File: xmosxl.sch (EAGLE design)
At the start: 1 part

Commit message: Add the block diagram
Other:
- note added: "!MPD!, !EXTSEL!"
- note added: "0.035mm"
- note added: "0.11mm pre-preg"
- note added: "0.12mm pre-preg"
- note added: "0.53mm pre-preg"
- note added: "177ns"
- note added: "225ns"
- note added: "3.96"
- note added: "4.29"
- note added: "422ns"
- note added: "486ns"
- note added: "Address,Data, Control from Mini-SAS"
- note added: "Atari Bus Mini-SAS (5v)"
- note added: "CLK"
- note added: "Cycle time = 558ns"
- note added: "Debug / XTAG / Link / UART"
- note added: "Dielectric constant"
- note added: "Expansion: bus + link (5w)"
- note added: "GND"
- note added: "I2C"
- note added: "Layer stack-up"
- note added: "Level Convert 5v <--> 3.3v"
- note added: "Per slot !IRQ!"
- note added: "Read"
- note added: "Shared A/D/State bus"
- note added: "Shared SPI / SS per slot"
- note added: "Signal"
- note added: "Slots"
- note added: "UART"
- note added: "VDD"
- note added: "Valid address"
- note added: "Write"
- note added: "XMOS 4-tile CPU - 2-way link to debugger - 5-way link to expansion - I2C / Uart offered - A/D/Flags bus decodes A8 bus - Expansion connector - SPI interface to slots"
- note added: "miniPBI+ (5v)"

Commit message: Start to lay out the design. Add slots and holes to take up space, and start to populate the level converters / vregs
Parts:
- added A8_CONN: MINI-SAS, sjg-con:MINI-SAS
- added AUDIO: AUDIO, pinhead:PINHD-1X3
- added C1, C10, C11, C12, C13, C14, C15, C16, C17, C18, C19, C2, C20, C3, C4, C5, C51, C52, C6, C7, C8, C9: 0.1uF, rcl:C-EUC0201
- added C21, C22, C23, C24, C25, C26, C27, C28, C29, C30, C31, C32, C33, C34, C35, C36, C37, C38, C39, C40, C43: 0.1uF, rcl:C-EUC0402K
- added C41, C42, C44, C45, C47: 10uF, rcl:C-EUC0402K
- added C46, C48: 1uF, rcl:C-EUC0402K
- added C49: 0.1uF, rcl:C-EUC0402
- added C50: 120pF, rcl:C-EUC0402
- added H1, H2, H3, H4: MOUNT-HOLE3.2, holes:MOUNT-HOLE3.2
- added IC1, IC2, IC3, IC4, IC5, IC8, IC9: 74LVC1T45W6-7, samacsys:74LVC1T45W6-7
- added IC6, IC7: 74ALVC164245DGG_11, samacsys:74ALVC164245DGG_11
- added PJ-102AH: PJ-102AH, adafruit:2.1MMJACKTHM
- added R1, R11, R2, R3, R4, R5, R6, R7, R8, R9: 10K, rcl:R-EU_R0201
- added R10: 47K, rcl:R-EU_R0402
- added SLOT1, SLOT2, SLOT3, SLOT4, SLOT5, SLOT6: PCIE_64, pcie:PCIE_64
- added U$2: AP7363-330-13, sjg-power:AP7363
- added U$3: LD49300, sjg-power:LD49150
- added U$4: TPS3808G33DBVR, sjg-power:TPS3808DBVR
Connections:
- new net !EXTSEL!: IC9.B
- new net !EXTSEL!_DIR: IC9.DIR, R11.2
- new net !HALT!: IC4.B
- new net !HALT!_DIR: IC4.DIR, R7.1
- new net !HI_EXTSEL!: A8_CONN.B13, IC9.A
- new net !HI_HALT!: A8_CONN.A14, IC4.A
- new net !HI_IRQ!: A8_CONN.B14, IC3.A
- new net !HI_MPD!: A8_CONN.A15, IC5.A
- new net !HI_REF!: A8_CONN.B16, IC8.A
- new net !HI_RST!: A8_CONN.A17, IC2.A
- new net !IRQ!: IC3.B
- new net !IRQ!_DIR: IC3.DIR, R6.1
- new net !MPD!: IC5.B
- new net !MPD!_DIR: IC5.DIR, R8.1
- new net !REF!: IC8.B
- new net !REF!_DIR: IC8.DIR, R9.1
- new net !RST!: IC2.B
- new net !RST!_DIR: IC2.DIR, R5.1
- new net +3V3: C10.1, C14.1, C15.1, C16.1, C19.1, C20.1, C21.1, C22.1, C23.1, C24.1, C25.1, C26.1, C27.1, C28.1, C41.1, C43.1, C45.1, C49.1, C52.1, C6.1, C7.1, C8.1, C9.1, IC1.VCC(B), IC2.VCC(B), IC3.VCC(B), IC4.VCC(B), IC5.VCC(B), IC6.VCC(A)@31, IC6.VCC(A)@42, IC7.VCC(A)@31, IC7.VCC(A)@42, IC8.VCC(B), IC9.VCC(B), R1.2, R10.2, R11.1, R5.2, R6.2, R7.2, R8.2, R9.2, U$1-POWER.VDDIO@A11, U$1-POWER.VDDIO@A2, U$1-POWER.VDDIO@A20, U$1-POWER.VDDIO@AA11, U$1-POWER.VDDIO@AA2, U$1-POWER.VDDIO@AA20, U$1-POWER.VDDIO@D7, U$1-POWER.VDDIO@E15, U$1-POWER.VDDIO@E7, U$1-POWER.VDDIO@F2, U$1-POWER.VDDIO@F20, U$1-POWER.VDDIO@L1, U$1-POWER.VDDIO@L21, U$1-POWER.VDDIO@T2, U$1-POWER.VDDIO@T20, U$1-POWER.VDDIO@U11, U$1-POWER.VDDIO@U15, U$1-POWER.VDDIO@U7, U$1-POWER.VDDIOT@A16, U$1-POWER.VDDIOT@A6, U$2.OUT@3, U$4.SENSE@5, U$4.VDD@6
- new net +5V: C1.1, C11.1, C12.1, C13.1, C17.1, C18.1, C2.1, C3.1, C4.1, C44.1, C46.1, C48.1, C5.1, C51.1, IC1.VCC(A), IC2.VCC(A), IC3.VCC(A), IC4.VCC(A), IC5.VCC(A), IC6.VCC(B)@18, IC6.VCC(B)@7, IC7.VCC(B)@18, IC7.VCC(B)@7, IC8.VCC(A), IC9.VCC(A), PJ-102AH.TIP, U$2.IN@1, U$3.VBIAS, U$3.VIN
- new net A0: IC7.1A0
- new net A1: IC7.1A1
- new net A10: IC7.2A2
- new net A11: IC7.2A3
- new net A12: IC7.2A4
- new net A13: IC7.2A5
- new net A14: IC7.2A6
- new net A15: IC7.2A7
- new net A2: IC7.1A2
- new net A3: IC7.1A3
- new net A4: IC7.1A4
- new net A5: IC7.1A5
- new net A6: IC7.1A6
- new net A7: IC7.1A7
- new net A8: IC7.2A0
- new net A9: IC7.2A1
- new net AUDIO_L: A8_CONN.B18, AUDIO.3
- new net AUDIO_R: A8_CONN.A18, AUDIO.1
- new net A_DIR: IC7.1DIR, IC7.2DIR, R2.1
- new net CLK: IC6.2A2
- new net CTRL_DIR: IC6.2DIR, R4.1
- new net D0: IC6.1A0
- new net D1: IC6.1A1
- new net D2: IC6.1A2
- new net D3: IC6.1A3
- new net D4: IC6.1A4
- new net D5: IC6.1A5
- new net D6: IC6.1A6
- new net D7: IC6.1A7
- new net D_DIR: IC6.1DIR, R3.1
- new net EN_1V0: R10.1, U$3.EN, U$4.!RESET!@1
- new net GND: A8_CONN.SHIELD, AUDIO.2, C1.2, C10.2, C11.2, C12.2, C13.2, C14.2, C15.2, C16.2, C17.2, C18.2, C19.2, C2.2, C20.2, C21.2, C22.2, C23.2, C24.2, C25.2, C26.2, C27.2, C28.2, C29.2, C3.2, C30.2, C31.2, C32.2, C33.2, C34.2, C35.2, C36.2, C37.2, C38.2, C39.2, C4.2, C40.2, C41.2, C42.2, C43.2, C44.2, C45.2, C46.2, C47.2, C48.2, C49.2, C5.2, C50.2, C51.2, C52.2, C6.2, C7.2, C8.2, C9.2, IC1.GND, IC2.GND, IC3.GND, IC4.GND, IC5.GND, IC6.!1OE, IC6.!2OE, IC6.2A3, IC6.2A4, IC6.2A5, IC6.2A6, IC6.2A7, IC6.2B3, IC6.2B4, IC6.2B5, IC6.2B6, IC6.2B7, IC6.GND@10, IC6.GND@15, IC6.GND@21, IC6.GND@28, IC6.GND@34, IC6.GND@39, IC6.GND@4, IC6.GND@45, IC7.!1OE, IC7.!2OE, IC7.GND@10, IC7.GND@15, IC7.GND@21, IC7.GND@28, IC7.GND@34, IC7.GND@39, IC7.GND@4, IC7.GND@45, IC8.GND, IC9.GND, PJ-102AH.RING, R2.2, R3.2, R4.2, U$1-POWER.GND@A1, U$1-POWER.GND@A21, U$1-POWER.GND@AA1, U$1-POWER.GND@AA21, U$1-POWER.GND@B11, U$1-POWER.GND@C15, U$1-POWER.GND@C7, U$1-POWER.GND@D6, U$1-POWER.GND@E16, U$1-POWER.GND@E6, U$1-POWER.GND@F19, U$1-POWER.GND@F3, U$1-POWER.GND@J13, U$1-POWER.GND@J14, U$1-POWER.GND@J15, U$1-POWER.GND@J16, U$1-POWER.GND@J17, U$1-POWER.GND@J5, U$1-POWER.GND@J6, U$1-POWER.GND@J7, U$1-POWER.GND@J8, U$1-POWER.GND@J9, U$1-POWER.GND@K13, U$1-POWER.GND@K14, U$1-POWER.GND@K15, U$1-POWER.GND@K16, U$1-POWER.GND@K17, U$1-POWER.GND@K5, U$1-POWER.GND@K6, U$1-POWER.GND@K7, U$1-POWER.GND@K8, U$1-POWER.GND@K9, U$1-POWER.GND@L13, U$1-POWER.GND@L14, U$1-POWER.GND@L15, U$1-POWER.GND@L16, U$1-POWER.GND@L17, U$1-POWER.GND@L2, U$1-POWER.GND@L20, U$1-POWER.GND@L5, U$1-POWER.GND@L6, U$1-POWER.GND@L7, U$1-POWER.GND@L8, U$1-POWER.GND@L9, U$1-POWER.GND@M13, U$1-POWER.GND@M14, U$1-POWER.GND@M15, U$1-POWER.GND@M16, U$1-POWER.GND@M17, U$1-POWER.GND@M5, U$1-POWER.GND@M6, U$1-POWER.GND@M7, U$1-POWER.GND@M8, U$1-POWER.GND@M9, U$1-POWER.GND@N13, U$1-POWER.GND@N14, U$1-POWER.GND@N15, U$1-POWER.GND@N16, U$1-POWER.GND@N17, U$1-POWER.GND@N5, U$1-POWER.GND@N6, U$1-POWER.GND@N7, U$1-POWER.GND@N8, U$1-POWER.GND@N9, U$1-POWER.GND@T11, U$1-POWER.GND@T19, U$1-POWER.GND@T3, U$1-POWER.GND@U16, U$1-POWER.GND@U6, U$1-POWER.GND@W15, U$1-POWER.GND@W7, U$1-POWER.GND@Y11, U$2.GND@2, U$3.GND, U$4.GND@2
- new net HI_A0: A8_CONN.A1, IC7.1B0
- new net HI_A1: A8_CONN.B1, IC7.1B1
- new net HI_A10: A8_CONN.A6, IC7.2B2
- new net HI_A11: A8_CONN.B6, IC7.2B3
- new net HI_A12: A8_CONN.A7, IC7.2B4
- new net HI_A13: A8_CONN.B7, IC7.2B5
- new net HI_A14: A8_CONN.A8, IC7.2B6
- new net HI_A15: A8_CONN.B8, IC7.2B7
- new net HI_A2: A8_CONN.A2, IC7.1B2
- new net HI_A3: A8_CONN.B2, IC7.1B3
- new net HI_A4: A8_CONN.A3, IC7.1B4
- new net HI_A5: A8_CONN.B3, IC7.1B5
- new net HI_A6: A8_CONN.A4, IC7.1B6
- new net HI_A7: A8_CONN.B4, IC7.1B7
- new net HI_A8: A8_CONN.A5, IC7.2B0
- new net HI_A9: A8_CONN.B5, IC7.2B1
- new net HI_CLK: A8_CONN.A13, IC6.2B2
- new net HI_D0: A8_CONN.A9, IC6.1B0
- new net HI_D1: A8_CONN.B9, IC6.1B1
- new net HI_D2: A8_CONN.A10, IC6.1B2
- new net HI_D3: A8_CONN.B10, IC6.1B3
- new net HI_D4: A8_CONN.A11, IC6.1B4
- new net HI_D5: A8_CONN.B11, IC6.1B5
- new net HI_D6: A8_CONN.A12, IC6.1B6
- new net HI_D7: A8_CONN.B12, IC6.1B7
- new net HI_R/!W!: A8_CONN.B17, IC1.A
- new net HI_RD4: A8_CONN.B15, IC6.2B1
- new net HI_RD5: A8_CONN.A16, IC6.2B0
- new net N$5: C50.1, U$4.CT@4
- new net R/!W!: IC1.B
- new net R/!W!_DIR: IC1.DIR, R1.1
- new net RD4: IC6.2A1
- new net RD5: IC6.2A0
- new net VDD: C29.1, C30.1, C31.1, C32.1, C33.1, C34.1, C35.1, C36.1, C37.1, C38.1, C39.1, C40.1, C42.1, C47.1, U$1-POWER.VDD@C19, U$1-POWER.VDD@C3, U$1-POWER.VDD@E13, U$1-POWER.VDD@E14, U$1-POWER.VDD@E17, U$1-POWER.VDD@E18, U$1-POWER.VDD@E4, U$1-POWER.VDD@E5, U$1-POWER.VDD@E8, U$1-POWER.VDD@E9, U$1-POWER.VDD@F12, U$1-POWER.VDD@F13, U$1-POWER.VDD@F14, U$1-POWER.VDD@F15, U$1-POWER.VDD@F16, U$1-POWER.VDD@F17, U$1-POWER.VDD@F18, U$1-POWER.VDD@F4, U$1-POWER.VDD@F5, U$1-POWER.VDD@F6, U$1-POWER.VDD@F7, U$1-POWER.VDD@F8, U$1-POWER.VDD@F9, U$1-POWER.VDD@H19, U$1-POWER.VDD@H3, U$1-POWER.VDD@J19, U$1-POWER.VDD@J3, U$1-POWER.VDD@N19, U$1-POWER.VDD@N3, U$1-POWER.VDD@P19, U$1-POWER.VDD@P3, U$1-POWER.VDD@T10, U$1-POWER.VDD@T12, U$1-POWER.VDD@T13, U$1-POWER.VDD@T14, U$1-POWER.VDD@T16, U$1-POWER.VDD@T17, U$1-POWER.VDD@T18, U$1-POWER.VDD@T4, U$1-POWER.VDD@T5, U$1-POWER.VDD@T6, U$1-POWER.VDD@T8, U$1-POWER.VDD@T9, U$1-POWER.VDD@U13, U$1-POWER.VDD@U14, U$1-POWER.VDD@U17, U$1-POWER.VDD@U18, U$1-POWER.VDD@U4, U$1-POWER.VDD@U5, U$1-POWER.VDD@U9, U$3.VOUT
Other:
- note added: "3.3v from +5v"
- note added: "AP7363-330-13 : fixed, 3.3vout, 5.5vin, 1.5A"
- note added: "Gated 1v from +5v"
- note added: "Power entry"
- note added: "Regulated 5v supply at 10A. (JYH05010000B) Use copper strip 20mm wide to distribute to various vregs"
- note added: "Sequence 1v ramp to start 1.2ms after VDDIO rail has already reached 3.3v"
- note added: "Vdd should supply 1.4A LD49300 : fixed, 1vout, 5.5vin, 3A"
- note added: "t(Delay) = 1.2ms"

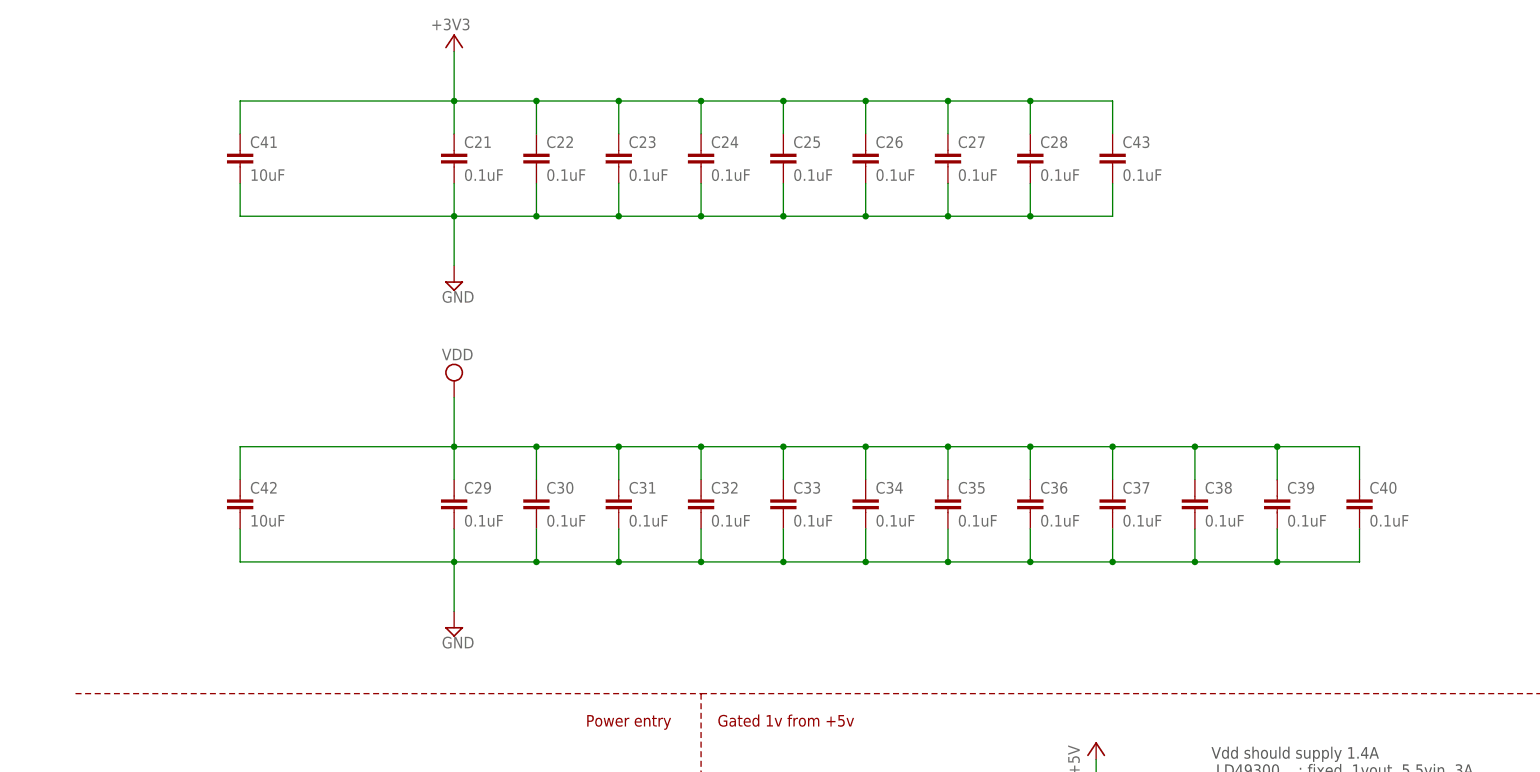
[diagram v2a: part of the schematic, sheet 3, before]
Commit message: Add the SDRAM and start on JTAG
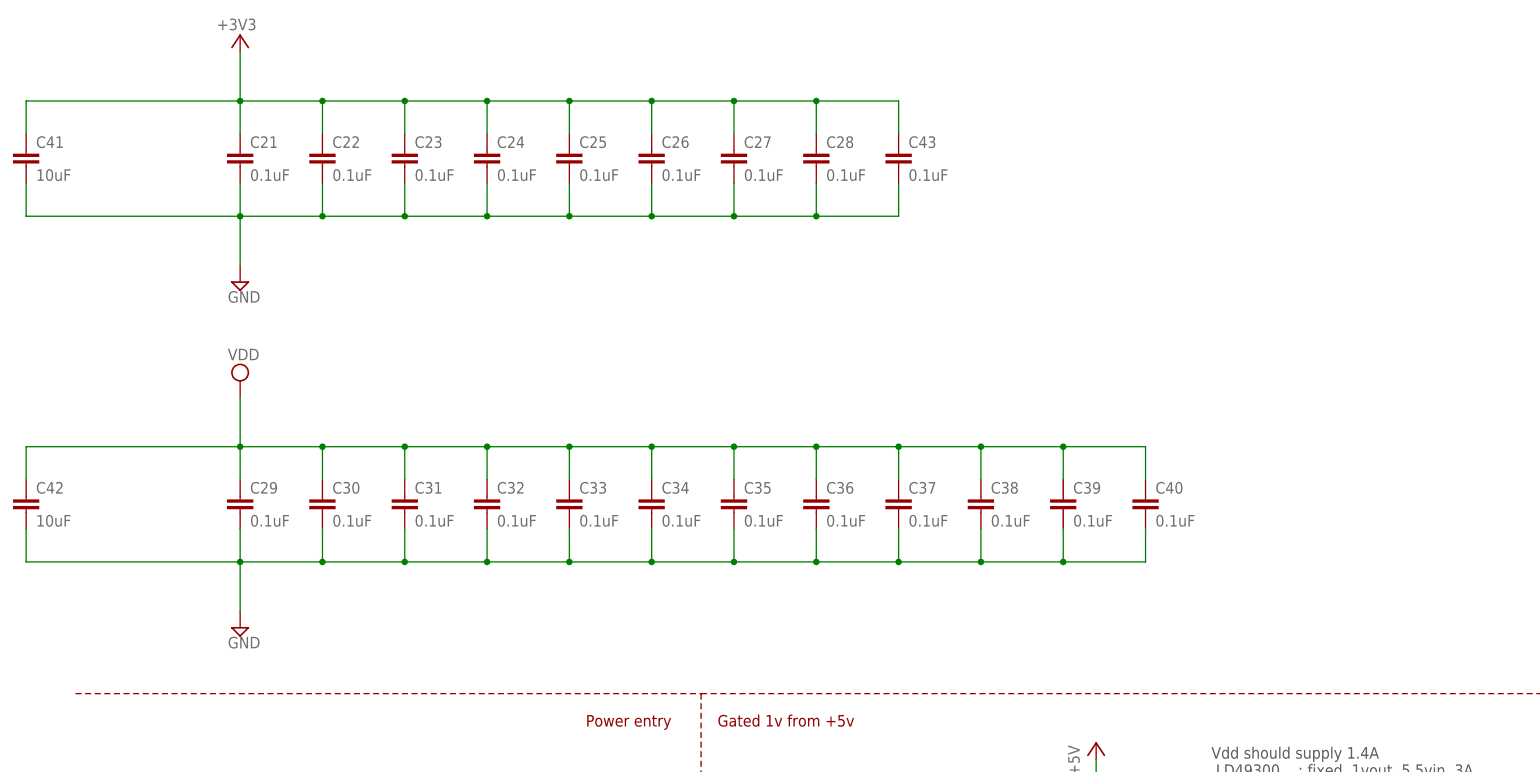
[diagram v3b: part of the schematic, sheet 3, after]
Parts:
- added C53: 10nF, rcl:C-EUC0201
- added C54, C55: 100nF, rcl:C-EUC1206
- added C56: 120pF, rcl:C-EUC1206
- added C57: 10nF, rcl:C-EUC1206
- added JTAG5V: PSU, pinhead:PINHD-1X2
- added NOR: SN74LVC1G02, sjg-logic:SN74LVC1G02
- added R12, R13: 10K, rcl:R-EU_R0201
- added R14, R15: 47K, rcl:R-EU_R1206
- added RESET_SW: MANUAL_RESET, SparkFun:TAC_SWITCHPTH
- added U$11: TPS3808G09DBVR, sjg-power:TPS3808G09DBVR
- added U$5: 74LVC1G07SE-7, sjg-logic:74LVC1G07SE-7
- added U$7: W9852G6KH, sjg-sdram:W9852G6KH
- added U1: 24 MHz Osc. (F535L-24), SparkFun:OSCILLATOR5X3-PIN1-INDICATED
- added XTAG: 1175-1618-ND, pinhead:PINHD-2X10/90
- C21, C22, C23, C24, C25, C26, C27, C28, C29, C30, C31, C32, C33, C34, C35, C36, C37, C38, C39, C40, C43: device rcl:C-EUC0402K -> rcl:C-EUC0201
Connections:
- new net !RESET!: R15.1, U$11.!RESET!@1, U$5.Y@4
- new net !SD_CAS!: NORG$1.I0, U$1-SDRAM.X2D20@Y18, U$7.!CAS!@17
- new net !SD_RAS!: U$1-SDRAM.X2D02@Y13, U$7.!RAS!@18
- new net !SD_WE!: NORG$1.I1, U$1-SDRAM.X2D21@AA18, U$7.!WE!@16
- new net JTAG_DN0: XTAG.14
- new net JTAG_DN1: XTAG.18
- new net JTAG_UP0: XTAG.10
- new net JTAG_UP1: XTAG.6
- new net N$1: R14.1, U$5.A@2, XTAG.15
- new net N$14: NORG$1.O, U$7.LDQM@15, U$7.UDQM@39
- new net N$15: R12.2, U$7.CKE@37
- new net N$17: R13.2, U$7.!CS!@19
- new net N$2: U$1-CTRL.CLK@A12, U1.OUT
- new net N$38: JTAG5V.2, XTAG.1
- new net N$4: C55.1, R15.2, U$11.VDD@6
- new net N$6: C56.1, U$11.CT@4
- new net N$7: C54.1
- new net N$8: R14.2, U$5.VCC@5
- new net SD_ADQ0: U$1-SDRAM.X2D03@AA13, U$7.A0@23, U$7.DQ0@2
- new net SD_ADQ1: U$1-SDRAM.X2D04@W13, U$7.A1@24, U$7.DQ1@4
- new net SD_ADQ10: U$1-SDRAM.X2D14@Y17, U$7.A10/AP@22, U$7.DQ10@45
- new net SD_ADQ11: U$1-SDRAM.X2D15@AA17, U$7.A11@35, U$7.DQ11@47
- new net SD_ADQ12: U$1-SDRAM.X2D16@W21, U$7.A12@36, U$7.DQ12@48
- new net SD_ADQ13: U$1-SDRAM.X2D17@V20, U$7.BS0@20, U$7.DQ13@50
- new net SD_ADQ14: U$1-SDRAM.X2D18@V21, U$7.BS1@21, U$7.DQ14@51
- new net SD_ADQ15: U$1-SDRAM.X2D19@U20, U$7.DQ15@53
- new net SD_ADQ2: U$1-SDRAM.X2D05@V13, U$7.A2@25, U$7.DQ2@5
- new net SD_ADQ3: U$1-SDRAM.X2D06@W14, U$7.A3@26, U$7.DQ3@7
- new net SD_ADQ4: U$1-SDRAM.X2D07@V14, U$7.A4@29, U$7.DQ4@8
- new net SD_ADQ5: U$1-SDRAM.X2D08@Y14, U$7.A5@30, U$7.DQ5@10
- new net SD_ADQ6: U$1-SDRAM.X2D09@AA14, U$7.A6@31, U$7.DQ6@11
- new net SD_ADQ7: U$1-SDRAM.X2D11@Y12, U$7.A7@32, U$7.DQ7@13
- new net SD_ADQ8: U$1-SDRAM.X2D12@V19, U$7.A8@33, U$7.DQ8@42
- new net SD_ADQ9: U$1-SDRAM.X2D13@Y20, U$7.A9@34, U$7.DQ9@44
- new net SD_CLK: U$1-SDRAM.X2D00@W12, U$7.CLK@38
- new net TCK: U$1-CTRL.TCK@B13, XTAG.9
- new net TDI: U$1-CTRL.TDI@A10, XTAG.5
- new net TDO: U$1-CTRL.TDO@A13, XTAG.13
- new net TMS: U$1-CTRL.TMS@D12, XTAG.7
- new net TRST_N: C57.2, RESET_SW.1, RESET_SW.2, U$11.!MR!@3
- new net UART_RX: XTAG.19
- new net UART_TX: XTAG.17
- net +3V3: now also C53.2, NORG$2.VCC, R12.1, U$7.VDD@1, U$7.VDD@14, U$7.VDD@27, U$7.VDDQ@3, U$7.VDDQ@43, U$7.VDDQ@49, U$7.VDDQ@9, U1.VCC
- net +5V: now also JTAG5V.1
- net GND: now also C53.1, C54.2, C55.2, C56.2, C57.1, NORG$2.GND, R13.1, RESET_SW.3, RESET_SW.4, U$11.GND@2, U$5.GND@3, U$7.VSS@28, U$7.VSS@41, U$7.VSS@54, U$7.VSSQ@12, U$7.VSSQ@46, U$7.VSSQ@52, U$7.VSSQ@6, U1.GND, XTAG.12, XTAG.16, XTAG.20, XTAG.4, XTAG.8
- net VDD: now also U$11.SENSE@5
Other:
- note added: "Clock is 24 MHz (within PLL range)"
- note added: "W9825G6KH"
- moved on the sheet: C21, C22, C23, C24, C25, C26, C27, C28, C29, C30, C31, C32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

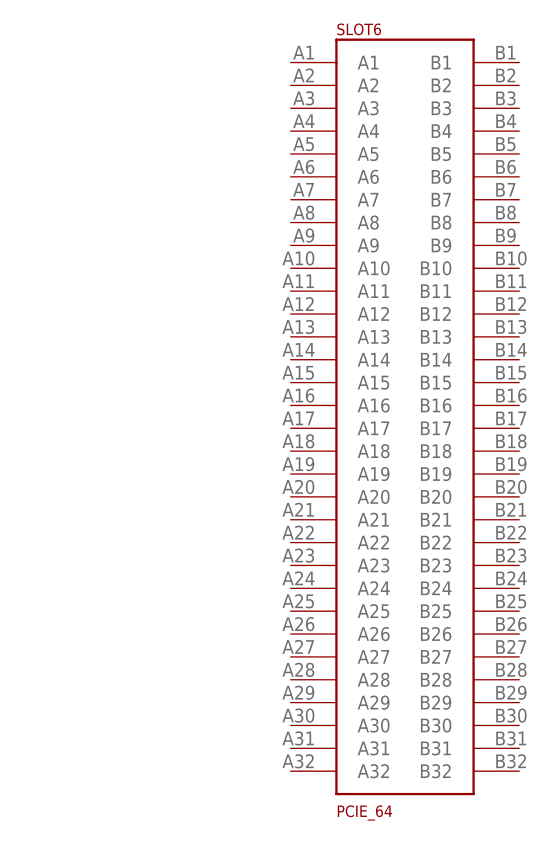
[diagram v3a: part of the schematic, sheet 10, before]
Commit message: Remove a slot - left with 5. Can add an “expansion box” for the remaining 5.
Add the JTAG link.
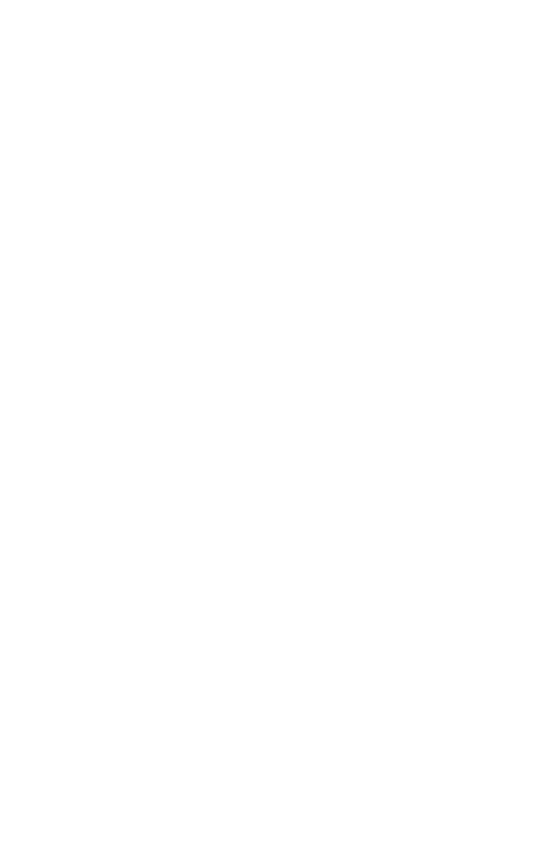
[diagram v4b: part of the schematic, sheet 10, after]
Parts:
- removed SLOT6: PCIE_64, pcie:PCIE_64
- added R16, R17: 33R, rcl:R-EU_R0201
- C54, C55: value 100nF -> 0.1uF; device rcl:C-EUC1206 -> rcl:C-EUC0201
- C56, C57: device rcl:C-EUC1206 -> rcl:C-EUC0201
- R14, R15: device rcl:R-EU_R1206 -> rcl:R-EU_R0201
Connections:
- removed net N$4: C55.1, R15.2, U$11.VDD@6
- removed net N$7: C54.1
- new net N$22: R16.1, U$1-LINK.X1D18@V2
- new net N$23: R17.1, U$1-LINK.X1D19@V1
- net +3V3: now also C54.1, C55.1, R15.2, U$11.VDD@6
- net JTAG_DN0: now also U$1-LINK.X1D17@U1
- net JTAG_DN1: now also U$1-LINK.X1D16@U2
- net JTAG_UP0: now also R16.2
- net JTAG_UP1: now also R17.2
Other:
- moved on the sheet: C55, C57, RESET_SW

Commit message: Start work on the slots
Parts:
- added C58: 0.1uF, rcl:C-EUC0201
- added DBG0, DBG1, DBG2, DBG3: ok33, led:LEDCHIP-LED0603
- added R18, R19, R22, R23, R25, R26: 10K, rcl:R-EU_R0201
- added R20, R21, R55, R56: 1K, rcl:R-EU_R0201
- added R24: 2.2R, rcl:R-EU_R0201
- renumbered U$1 to XMOS
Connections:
- new net !DEBUG!: XMOS-CTRL.!DEBUG!@D9, XTAG.11
- new net N$10: R26.2, XMOS-CTRL.MODE0@D10
- new net N$16: DBG0.C, R21.2
- new net N$18: DBG3.C, R55.2
- new net N$19: DBG1.C, R20.2
- new net N$3: DBG2.C, R56.2
- new net N$4: DBG0.A, XMOS-LED.X3D43@C16
- new net N$56: DBG1.A, XMOS-LED.X3D42@D16
- new net N$57: DBG2.A, XMOS-LED.X3D41@C17
- new net N$63: DBG3.A, XMOS-LED.X3D40@D17
- new net N$7: C58.1, R24.2, XMOS-POWER.PLL_AVDD@F11
- new net N$9: R25.1, XMOS-CTRL.MODE1@C10
- new net SBUS_A0: XMOS-SLOTBUS.X1D26@A5
- new net SBUS_A1: XMOS-SLOTBUS.X1D27@B5
- new net SBUS_A10: XMOS-SLOTBUS.X1D38@T1
- new net SBUS_A11: XMOS-SLOTBUS.X1D39@U3
- new net SBUS_A12: XMOS-SLOTBUS.X1D40@B7
- new net SBUS_A13: XMOS-SLOTBUS.X1D41@A7
- new net SBUS_A14: XMOS-SLOTBUS.X1D42@B6
- new net SBUS_A15: XMOS-SLOTBUS.X1D43@C6
- new net SBUS_A2: XMOS-SLOTBUS.X1D28@C5
- new net SBUS_A3: XMOS-SLOTBUS.X1D29@D5
- new net SBUS_A4: XMOS-SLOTBUS.X1D30@C4
- new net SBUS_A5: XMOS-SLOTBUS.X1D31@D4
- new net SBUS_A6: XMOS-SLOTBUS.X1D32@A4
- new net SBUS_A7: XMOS-SLOTBUS.X1D33@B4
- new net SBUS_A8: XMOS-SLOTBUS.X1D36@F1
- new net SBUS_A9: XMOS-SLOTBUS.X1D37@R3
- new net SBUS_CLK: XMOS-SLOTBUS.X1D21@AA8
- new net SBUS_D0: XMOS-SLOTBUS.X1D49@G1
- new net SBUS_D1: XMOS-SLOTBUS.X1D50@G2
- new net SBUS_D2: XMOS-SLOTBUS.X1D51@G3
- new net SBUS_D3: XMOS-SLOTBUS.X1D52@H2
- new net SBUS_D4: XMOS-SLOTBUS.X1D53@H1
- new net SBUS_D5: XMOS-SLOTBUS.X1D54@J1
- new net SBUS_D6: XMOS-SLOTBUS.X1D55@J2
- new net SBUS_D7: XMOS-SLOTBUS.X1D56@K3
- new net SBUS_FLG0: XMOS-SLOTBUS.X1D57@K2
- new net SBUS_FLG1: XMOS-SLOTBUS.X1D58@K1
- new net SBUS_FLG2: XMOS-SLOTBUS.X1D14@V8
- new net SBUS_FLG3: XMOS-SLOTBUS.X1D15@W8
- new net SBUS_FLG4: XMOS-SLOTBUS.X1D20@Y8
- new net SPI_BOPT0: XMOS-SPI.X0D14@W9
- new net SPI_BOPT1: XMOS-SPI.X0D15@Y9
- new net SPI_BOPT2: XMOS-SPI.X0D20@AA9
- new net SPI_BOPT3: XMOS-SPI.X0D21@V10
- new net SPI_BSEL0: XMOS-SPI.X0D02@V4
- new net SPI_BSEL1: XMOS-SPI.X0D03@W4
- new net SPI_BSEL2: XMOS-SPI.X0D08@V5
- new net SPI_BSEL3: XMOS-SPI.X0D09@W5
- new net SPI_CLK0: XMOS-SPI.X0D00@Y2
- new net SPI_CLK1: XMOS-SPI.X1D22@W2
- new net SPI_IRQ0: XMOS-SPI.X0D28@B9
- new net SPI_IRQ1: XMOS-SPI.X0D29@A9
- new net SPI_IRQ2: XMOS-SPI.X0D30@B8
- new net SPI_IRQ3: XMOS-SPI.X0D31@A8
- new net SPI_IRQ4: XMOS-SPI.X0D32@C9
- new net SPI_IRQ5: XMOS-SPI.X0D33@C8
- new net SPI_IRQ6: XMOS-SPI.X0D40@D2
- new net SPI_IRQ7: XMOS-SPI.X0D41@D1
- new net SPI_IRQ8: XMOS-SPI.X0D42@E2
- new net SPI_IRQ9: XMOS-SPI.X0D43@E1
- new net SPI_MISO0: XMOS-SPI.X0D11@V6
- new net SPI_MISO1: XMOS-SPI.X1D23@Y1
- new net SPI_MOSI0: XMOS-SPI.X0D12@W10
- new net SPI_MOSI1: XMOS-SPI.X1D24@Y7
- new net SPI_SS0: XMOS-SPI.X0D13@Y10
- new net SPI_SS1: XMOS-SPI.X0D22@AA10
- new net SPI_SS2: XMOS-SPI.X0D23@W11
- new net SPI_SS3: XMOS-SPI.X0D36@B2
- new net SPI_SS4: XMOS-SPI.X0D37@B1
- new net SPI_SS5: XMOS-SPI.X0D38@C2
- new net SPI_SS6: XMOS-SPI.X0D39@C1
- new net SPI_SS7: XMOS-SPI.X1D12@Y5
- new net SPI_SS8: XMOS-SPI.X1D13@AA5
- new net SPI_SS9: XMOS-SPI.X1D25@V9
- net !EXTSEL!: now also XMOS-A8BUS.X2D24@D21
- net !EXTSEL!_DIR: now also XMOS-A8BUS.X3D33@B14
- net !HALT!: now also XMOS-A8BUS.X2D36@B10
- net !HALT!_DIR: now also XMOS-A8BUS.X3D29@C14
- net !IRQ!: now also XMOS-A8BUS.X2D35@B21
- net !IRQ!_DIR: now also XMOS-A8BUS.X3D28@D14
- net !MPD!: now also XMOS-A8BUS.X2D25@C20
- net !MPD!_DIR: now also XMOS-A8BUS.X3D25@AA19
- net !REF!: now also XMOS-A8BUS.X3D23@V12
- net !REF!_DIR: now also XMOS-A8BUS.X3D30@A15
- net !RESET!: now also XMOS-CTRL.!RST!@B12, XMOS-CTRL.!TRST!@C12
- net !RST!: now also XMOS-A8BUS.X2D34@C21
- net !RST!_DIR: now also XMOS-A8BUS.X3D27@B16
- net +3V3: now also R18.1, R25.2, XMOS-POWER.OTP_VCC@C11
- net A0: now also XMOS-A8BUS.X2D49@R19
- net A1: now also XMOS-A8BUS.X2D50@N20
- net A10: now also XMOS-A8BUS.X2D61@J21
- net A11: now also XMOS-A8BUS.X2D62@J20
- net A12: now also XMOS-A8BUS.X2D63@H20
- net A13: now also XMOS-A8BUS.X2D64@H21
- net A14: now also XMOS-A8BUS.X2D65@G21
- net A15: now also XMOS-A8BUS.X2D66@G20
- net A2: now also XMOS-A8BUS.X2D51@N21
- net A3: now also XMOS-A8BUS.X2D52@M21
- net A4: now also XMOS-A8BUS.X2D53@M20
- net A5: now also XMOS-A8BUS.X2D54@M19
- net A6: now also XMOS-A8BUS.X2D55@L19
- net A7: now also XMOS-A8BUS.X2D56@K19
- net A8: now also XMOS-A8BUS.X2D57@K20
- net A9: now also XMOS-A8BUS.X2D58@K21
- net A_DIR: now also XMOS-A8BUS.X3D31@B15
- net CLK: now also XMOS-A8BUS.X2D22@Y21
- net D0: now also XMOS-A8BUS.X2D26@B20
- net D1: now also XMOS-A8BUS.X2D27@B19
- net D2: now also XMOS-A8BUS.X2D28@B18
- net D3: now also XMOS-A8BUS.X2D29@A18
- net D4: now also XMOS-A8BUS.X2D30@B17
- net D5: now also XMOS-A8BUS.X2D31@A17
- net D6: now also XMOS-A8BUS.X2D32@A19
- net D7: now also XMOS-A8BUS.X2D33@C18
- net D_DIR: now also XMOS-A8BUS.X3D32@A14
- net GND: now also C58.2, R19.1, R20.1, R21.1, R22.1, R23.1, R26.1, R55.1, R56.1, XMOS-A8BUS.X2D67@G19, XMOS-A8BUS.X2D68@F21, XMOS-A8BUS.X2D69@E19, XMOS-A8BUS.X2D70@D18, XMOS-A8BUS.X3D14@W17, XMOS-A8BUS.X3D15@V17, XMOS-POWER.PLL_AGND@F10
- net R/!W!: now also XMOS-A8BUS.X2D23@W20
- net R/!W!_DIR: now also XMOS-A8BUS.X3D26@D15
- net RD4: now also XMOS-A8BUS.X3D20@W18
- net RD5: now also XMOS-A8BUS.X3D21@V18
- net SD_ADQ1: now also R19.2
- net SD_ADQ2: now also R22.2
- net SD_ADQ3: now also R18.2
- net SD_ADQ7: now also R23.2
- net VDD: now also R24.1
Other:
- note added: "Ports only source 4mA, so use 1K resistors"
